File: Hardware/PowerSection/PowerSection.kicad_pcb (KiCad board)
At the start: 2 copper layers, 79 x 63 mm, 39 parts, among them J1 JST-B5B-XH-A, J2 Conn_01x02_Pin, Q1 2N7002, Q2 CMD05N03A, U1 INA180B4, U2 INA180B1, U4 ZXGD3009DY

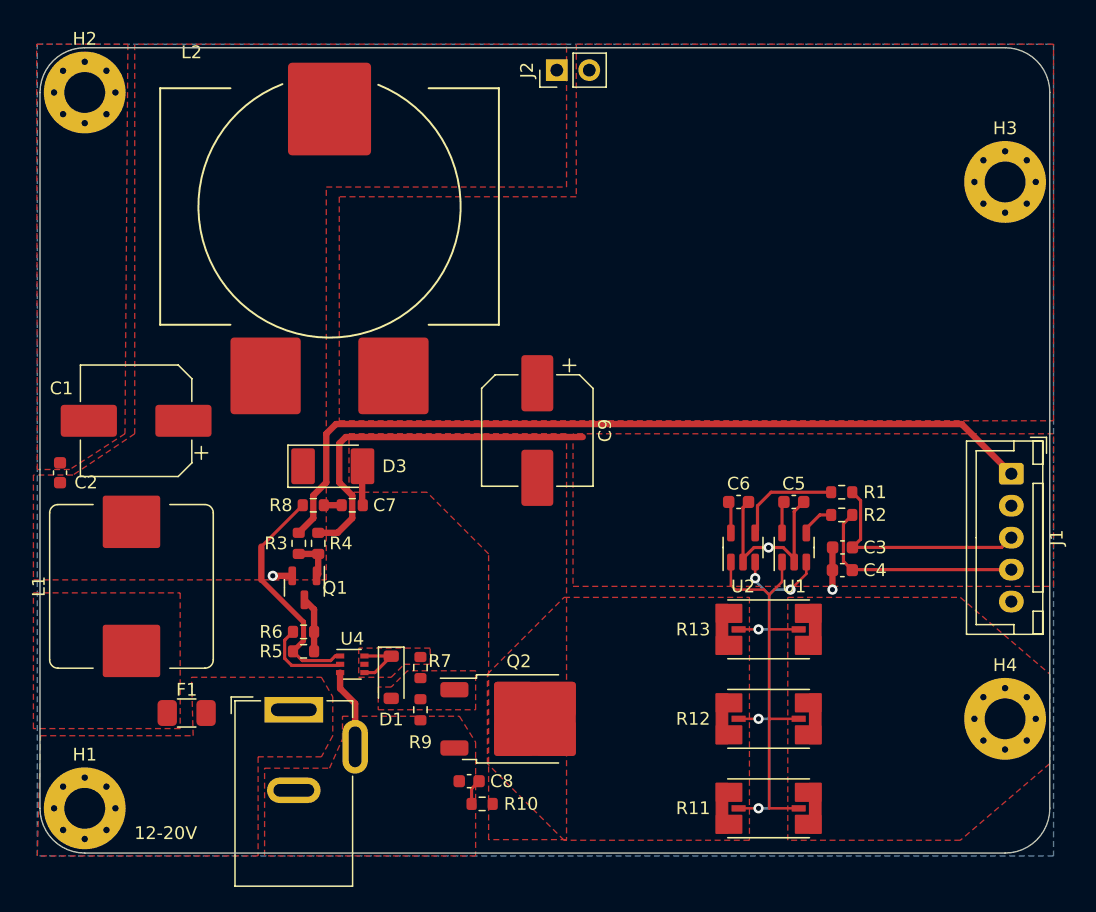
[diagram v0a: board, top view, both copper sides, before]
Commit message: Minor tweaks - labeling contacts and such.
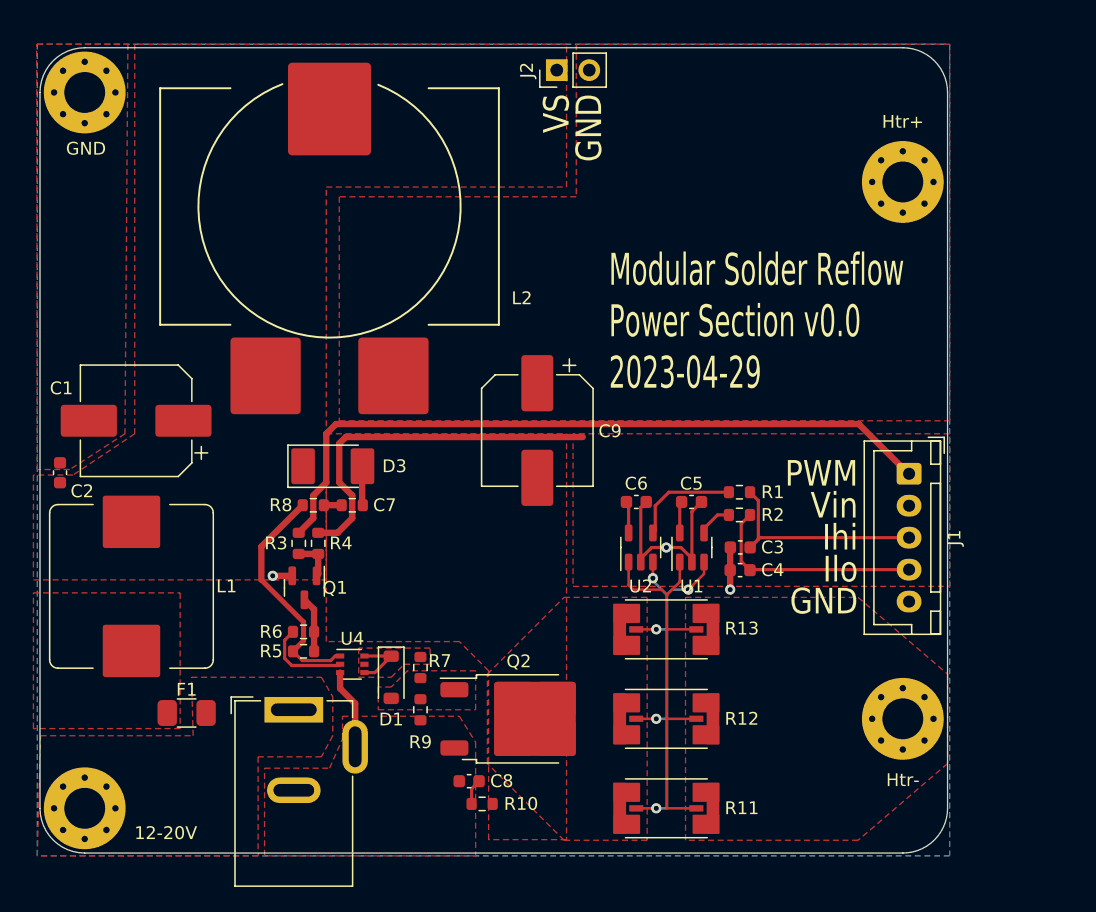
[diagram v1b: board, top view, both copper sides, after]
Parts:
- moved C3 8.00 mm to (152.8, 85.1)
- moved C4 8.00 mm to (152.8, 86.9)
- moved C5 8.00 mm to (149.0, 81.5)
- moved C6 8.00 mm to (144.7, 81.5)
- moved H3 8.00 mm to (165.5, 56.5)
- moved H4 8.00 mm to (165.5, 98.5)
- moved J1 8.00 mm to (166.0, 79.3)
- moved R1 8.00 mm to (152.7, 80.8)
- moved R11 8.00 mm to (147.0, 105.5)
- moved R12 8.00 mm to (147.0, 98.5)
- moved R13 8.00 mm to (147.0, 91.5)
- moved R2 8.00 mm to (152.7, 82.5)
- moved U1 8.00 mm to (149.0, 85.1)
- moved U2 8.00 mm to (145.0, 85.1)
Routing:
- net PWM: track 64.2 -> 56.2 mm
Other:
- board size 79 x 63 mm -> 71 x 63 mm
- board text added: "GND"
- board text added: "Ihi"
- board text added: "Ilo"
- board text added: "Modular Solder Reflow Power Section v0.0 2023-04-29"
- board text added: "PWM"
- board text added: "VS"
- board text added: "Vin"
